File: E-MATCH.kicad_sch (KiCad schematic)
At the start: 20 parts, among them IC1 NCV81071BZR2G, IC2 NCV81071BZR2G, J1 691210910002, J2 691210910002, J3 691210910002, J4 691210910002, Q1 AOSP36326C, Q2 AOSP36326C, Q3 AOSP36326C, Q4 AOSP36326C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

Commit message: routing
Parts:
- added J5: DC Jack, DC-Jack:TENSILITY_54-00130, symbol DC Jack:54-00130
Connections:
- net GND: now also J5.B, J5.C; no longer IC1.3 (ENB), IC1.4 (INB), IC2.3 (ENB), IC2.4 (INB)
- net Gate_Drive1: now also R1.2
- net Gate_Drive2: now also R2.2
- net Gate_Drive3: now also R3.2
- net Gate_Drive4: now also R4.2
- net VBAT: now also J5.A
- net Enable_Signal4: now reaches A1.11 (D8)
- net Enable_Signal4: now also IC2.3 (ENB)
- net Enable_Signal3: now reaches A1.12 (D9)
- net Enable_Signal3: now also IC2.1 (ENA)
- net Enable_Signal2: now reaches A1.13 (D10)
- net Enable_Signal2: now also IC1.3 (ENB)
- net Enable_Signal1: now reaches A1.14 (D11)
- net Enable_Signal1: now also IC1.1 (ENA)
- net Trigger_Signal4: now reaches A1.5 (D2)
- net Trigger_Signal4: now also IC2.4 (INB)
- net Trigger_Signal3: now reaches A1.6 (D3)
- net Trigger_Signal3: now also IC2.2 (INA)
- net Trigger_Signal2: now reaches A1.7 (D4)
- net Trigger_Signal2: now also IC1.4 (INB)
- removed net Enable_Signal: A1.10 (D7), IC1.1 (ENA), IC2.1 (ENA)
- net Trigger_Signal renamed Trigger_Signal1
- net Trigger_Signal1: no longer IC2.2 (INA)
- no-connect marks 1 -> 3
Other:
- note removed: "Arduino Nano(Micro Controller)"
- note removed: "CURRENT SENSOR"
- note removed: "GATE DRIVER IC"
- note removed: "Inputs"
- note removed: "Outputs"
- note removed: "SCHOTTCKY DIODE"
- moved on the sheet: A1, IC1, IC2, U1

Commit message: Led-indicator file structure
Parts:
- IC1: footprint Gate Driver:SOP65P490X110-9N -> SOP65P490X110-9N; Description_1 Low-Side Gate Driver IC CMOS, TTL 8-MSOP-EP -> (none)
- IC2: footprint Gate Driver:SOP65P490X110-9N -> SOP65P490X110-9N
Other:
- moved on the sheet: IC2

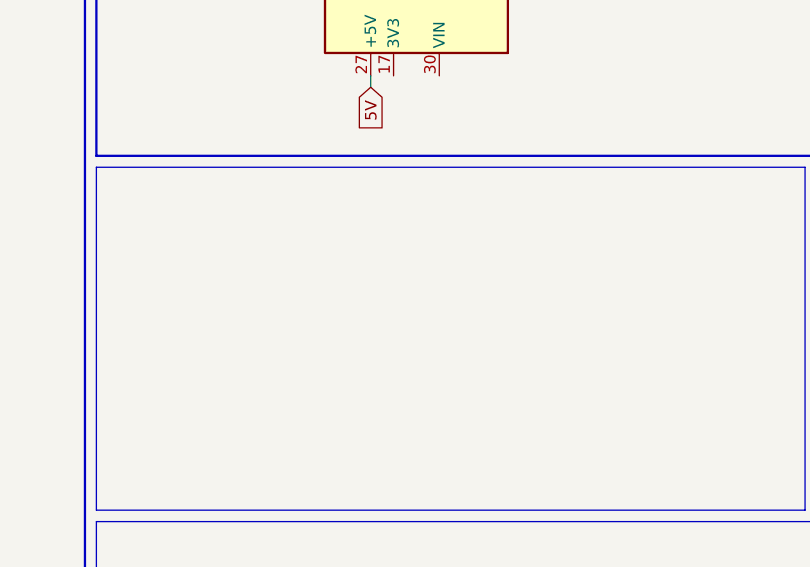
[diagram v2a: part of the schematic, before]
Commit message: Added SMD-LED footprint
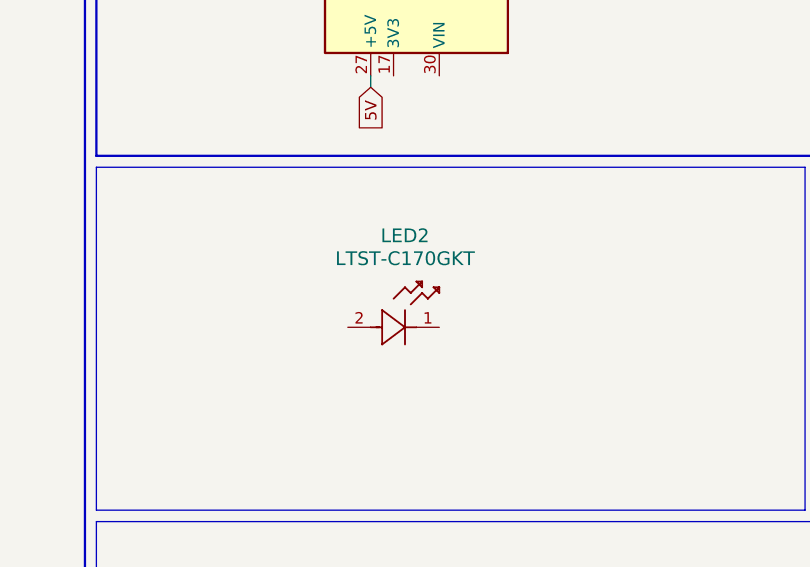
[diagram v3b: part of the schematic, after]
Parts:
- added LED2: LTST-C170GKT, LED_LTST-C170GKT_LTO, symbol LTST-C170GKT:LTST-C170GKT
- CR1, CR2, CR3, CR4: footprint DIODE_MSP3V3 -> (none)
- IC1, IC2: footprint SOP65P490X110-9N -> (none)
- Q1, Q2, Q3, Q4: footprint SO8SOP-8L_AOS -> (none)
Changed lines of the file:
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@@
 			)
 		)
-		(property "Footprint" "DIODE_MSP3V3"
+		(property "Footprint" ""
 			(at 68.58 99.06 0)
 			(effects
@@
 			)
 		)
-		(property "Footprint" "SOP65P490X110-9N"
+		(property "Footprint" ""
 			(at 254 139.37 0)
 			(effects
@@
 	)
 	(symbol
+		(lib_id "LTST-C170GKT:LTST-C170GKT")
+		(at 151.13 104.14 0)
+		(unit 1)
+		(exclude_from_sim no)
+		(in_bom yes)
+		(on_board yes)
+		(dnp no)
+		(fields_autoplaced yes)
+		(property "Reference" "LED2"
+			(at 157.48 93.98 0)
+			(effects
+				(font
+					(size 1.524 1.524)
+				)
+			)
+		)
+		(property "Value" "LTST-C170GKT"
+			(at 157.48 96.52 0)
+			(effects
+				(font
+					(size 1.524 1.524)
+				)
+			)
+		)
+		(property "Footprint" "LED_LTST-C170GKT_LTO"
+			(at 151.13 104.14 0)
+			(effects
+				(font
+					(size 1.27 1.27)
+					(italic yes)
+				)
+				(hide yes)
+			)
+		)
+		(property "Datasheet" "LTST-C170GKT"
+			(at 151.13 104.14 0)
+			(effects
+				(font
+					(size 1.27 1.27)
+					(italic yes)
+				)
+				(hide yes)
+			)
+		)
+		(property "Description" ""
+			(at 151.13 104.14 0)
+			(effects
+				(font
+					(size 1.27 1.27)
+				)
+				(hide yes)
+			)
+		)
+		(pin "1"
+		)
+		(pin "2"
+		)
+		(instances
+			(project ""
+				(path "/ac49d8b8-9946-4b6b-9646-a2b20606c52a"
+					(reference "LED2")
+					(unit 1)
+				)
+			)
+		)
+	)
+	(symbol
 		(lib_id "Schottcky Diode:MSS1P5-M3_89A")
 		(at 87.63 99.06 90)
@@
 			)
 		)
-		(property "Footprint" "DIODE_MSP3V3"
+		(property "Footprint" ""
 			(at 87.63 99.06 0)
 			(effects
@@
 			)
 		)
-		(property "Footprint" "DIODE_MSP3V3"
+		(property "Footprint" ""
 			(at 50.8 99.06 0)
 			(effects
@@
 			)
 		)
-		(property "Footprint" "SOP65P490X110-9N"
+		(property "Footprint" ""
 			(at 253.238 116.51 0)
 			(effects
@@
 			)
 		)
-		(property "Footprint" "DIODE_MSP3V3"
+		(property "Footprint" ""
 			(at 105.41 99.06 0)
 			(effects
@@
 			)
 		)
-		(property "Footprint" "SO8SOP-8L_AOS"
+		(property "Footprint" ""
 			(at 86.868 133.858 0)
 			(effects
@@
 			)
 		)
-		(property "Footprint" "SO8SOP-8L_AOS"
+		(property "Footprint" ""
 			(at 66.548 133.858 0)
 			(effects
@@
 			)
 		)
-		(property "Footprint" "SO8SOP-8L_AOS"
+		(property "Footprint" ""
 			(at 37.592 133.35 0)
 			(effects
@@
 			)
 		)
-		(property "Footprint" "SO8SOP-8L_AOS"
+		(property "Footprint" ""
 			(at 47.498 133.858 0)
 			(effects

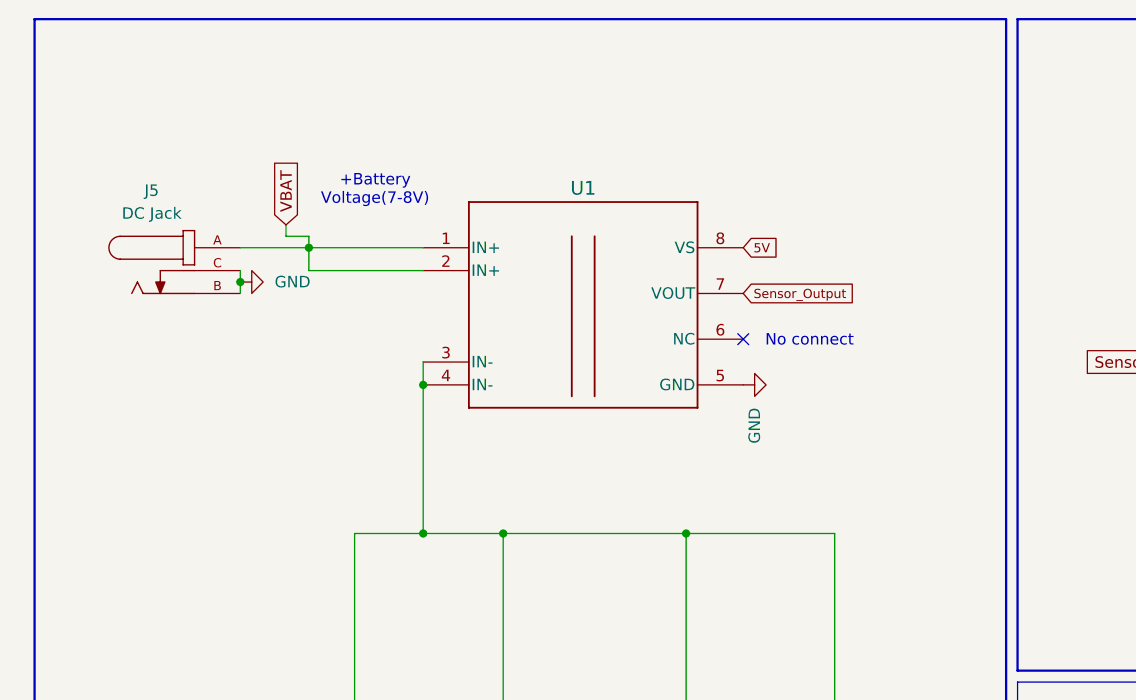
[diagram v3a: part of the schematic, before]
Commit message: edited current sensor symbol
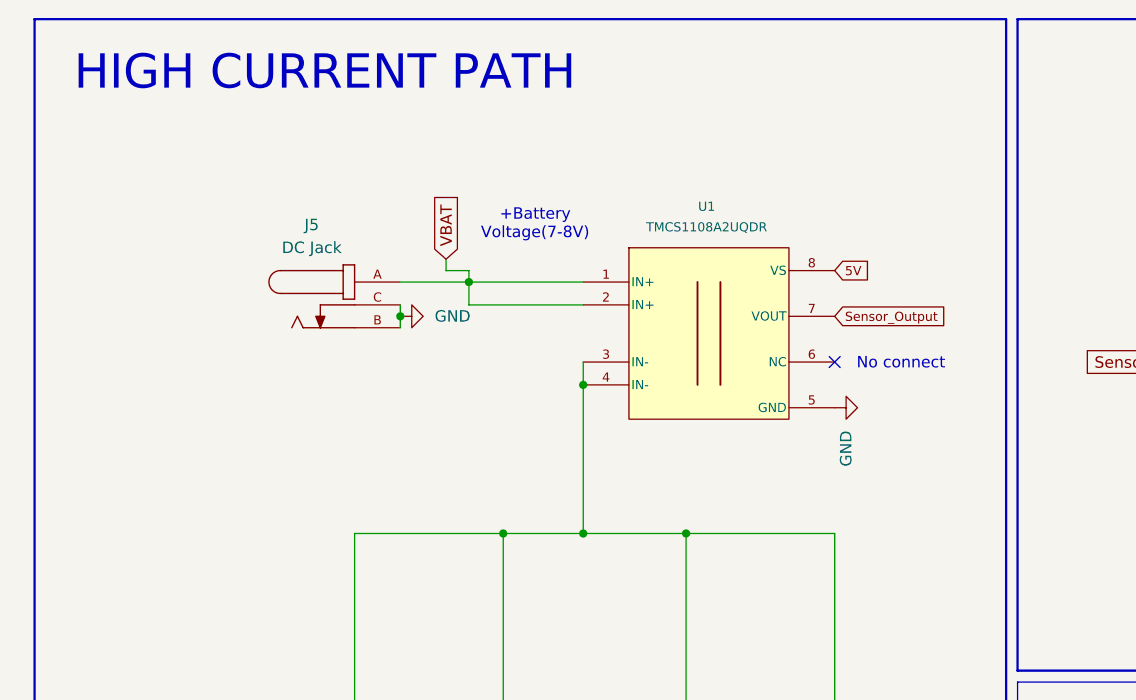
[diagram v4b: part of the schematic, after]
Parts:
- U1: footprint Current Sensor:D0008A-MFG -> D0008A-IPC_A
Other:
- note added: "HIGH CURRENT PATH"
- moved on the sheet: J5

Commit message: Schematic Cleanup
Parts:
- IC2: footprint (none) -> SOP65P490X110-9N
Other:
- note added: "GATE DRIVERS"
- note added: "MCU"
- note added: "Resistors to limit gate driving current to around 1 Ampere"
- note removed: "Resistor to limit gate driving current to around 1 Ampere"
- moved on the sheet: A1, CR1, CR2, CR3, CR4, IC1, IC2, J1, J2, J3, J4, J5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

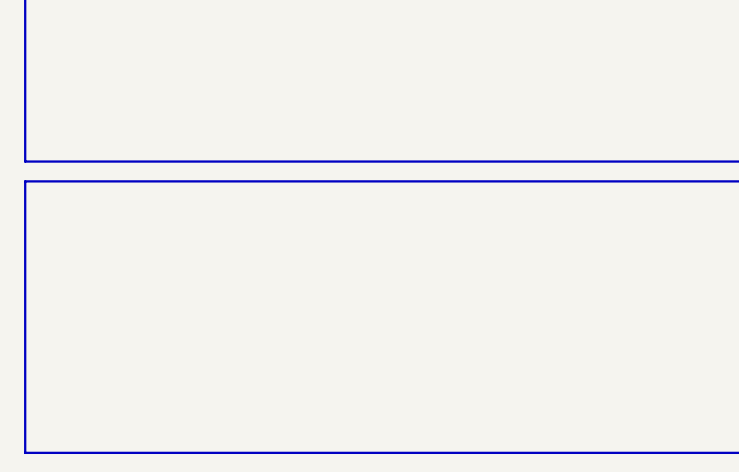
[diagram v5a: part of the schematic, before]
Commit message: SMD_Resistor added
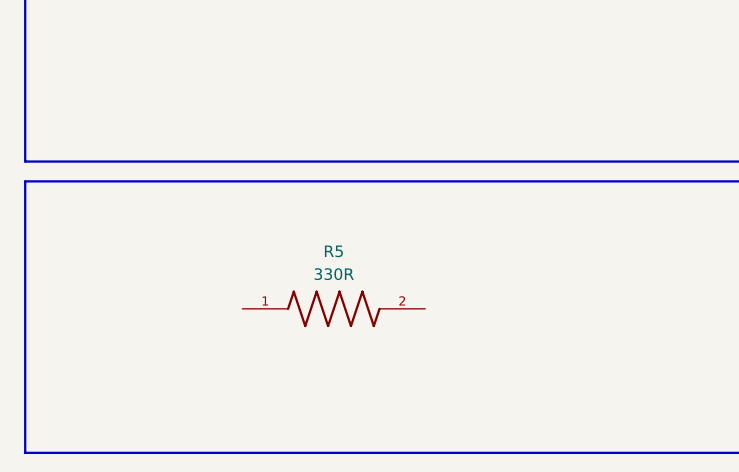
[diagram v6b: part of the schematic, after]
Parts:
- added R5: 330R, SMD_RESISTOR:RESC1608X55N, symbol RC0603JR-07330RL:RC0603JR-07330RL
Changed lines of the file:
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@@
+	)
+	(symbol
+		(lib_id "RC0603JR-07330RL:RC0603JR-07330RL")
+		(at 48.26 180.34 0)
+		(unit 1)
+		(exclude_from_sim no)
+		(in_bom yes)
+		(on_board yes)
+		(dnp no)
+		(fields_autoplaced yes)
+		(property "Reference" "R5"
+			(at 48.26 173.99 0)
+			(effects
+				(font
+					(size 1.27 1.27)
+				)
+			)
+		)
+		(property "Value" "330R"
+			(at 48.26 176.53 0)
+			(effects
+				(font
+					(size 1.27 1.27)
+				)
+			)
+		)
+		(property "Footprint" "SMD_RESISTOR:RESC1608X55N"
+			(at 48.26 180.34 0)
+			(effects
+				(font
+					(size 1.27 1.27)
+				)
+				(justify bottom)
+				(hide yes)
+			)
+		)
+		(property "Datasheet" ""
+			(at 48.26 180.34 0)
+			(effects
+				(font
+					(size 1.27 1.27)
+				)
+				(hide yes)
+			)
+		)
+		(property "Description" ""
+			(at 48.26 180.34 0)
+			(effects
+				(font
+					(size 1.27 1.27)
+				)
+				(hide yes)
+			)
+		)
+		(property "DigiKey_Part_Number" "311-330GRCT-ND"
+			(at 48.26 180.34 0)
+			(effects
+				(font
+					(size 1.27 1.27)
+				)
+				(justify bottom)
+				(hide yes)
+			)
+		)
+		(property "SnapEDA_Link" "https://www.snapeda.com/parts/RC0603JR-07330RL/Yageo/view-part/?ref=snap"
+			(at 48.26 180.34 0)
+			(effects
+				(font
+					(size 1.27 1.27)
+				)
+				(justify bottom)
+				(hide yes)
+			)
+		)
+		(property "Description_1" "330 Ohms ±5% 0.1W, 1/10W Chip Resistor 0603 (1608 Metric) Moisture Resistant Thick Film"
+			(at 48.26 180.34 0)
+			(effects
+				(font
+					(size 1.27 1.27)
+				)
+				(justify bottom)
+				(hide yes)
+			)
+		)
+		(property "MF" "Yageo"
+			(at 48.26 180.34 0)
+			(effects
+				(font
+					(size 1.27 1.27)
+				)
+				(justify bottom)
+				(hide yes)
+			)
+		)
+		(property "Package" "1608 Yageo"
+			(at 48.26 180.34 0)
+			(effects
+				(font
+					(size 1.27 1.27)
+				)
+				(justify bottom)
+				(hide yes)
+			)
+		)
+		(property "Check_prices" "https://www.snapeda.com/parts/RC0603JR-07330RL/Yageo/view-part/?ref=eda"
+			(at 48.26 180.34 0)
+			(effects
+				(font
+					(size 1.27 1.27)
+				)
+				(justify bottom)
+				(hide yes)
+			)
+		)
+		(property "MP" "RC0603JR-07330RL"
+			(at 48.26 180.34 0)
+			(effects
+				(font
+					(size 1.27 1.27)
+				)
+				(justify bottom)
+				(hide yes)
+			)
+		)
+		(pin "1"
+		)
+		(pin "2"
+		)
+		(instances
+			(project ""
+				(path "/ac49d8b8-9946-4b6b-9646-a2b20606c52a"
+					(reference "R5")
+					(unit 1)
+				)
+			)
+		)
 	)
 	(symbol
